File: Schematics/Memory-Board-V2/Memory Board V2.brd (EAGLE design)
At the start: 114 x 88.9 mm, 15 parts, among them IC4 27C128P, IC5 74HC174N, U1 GAL22V10D-DIP

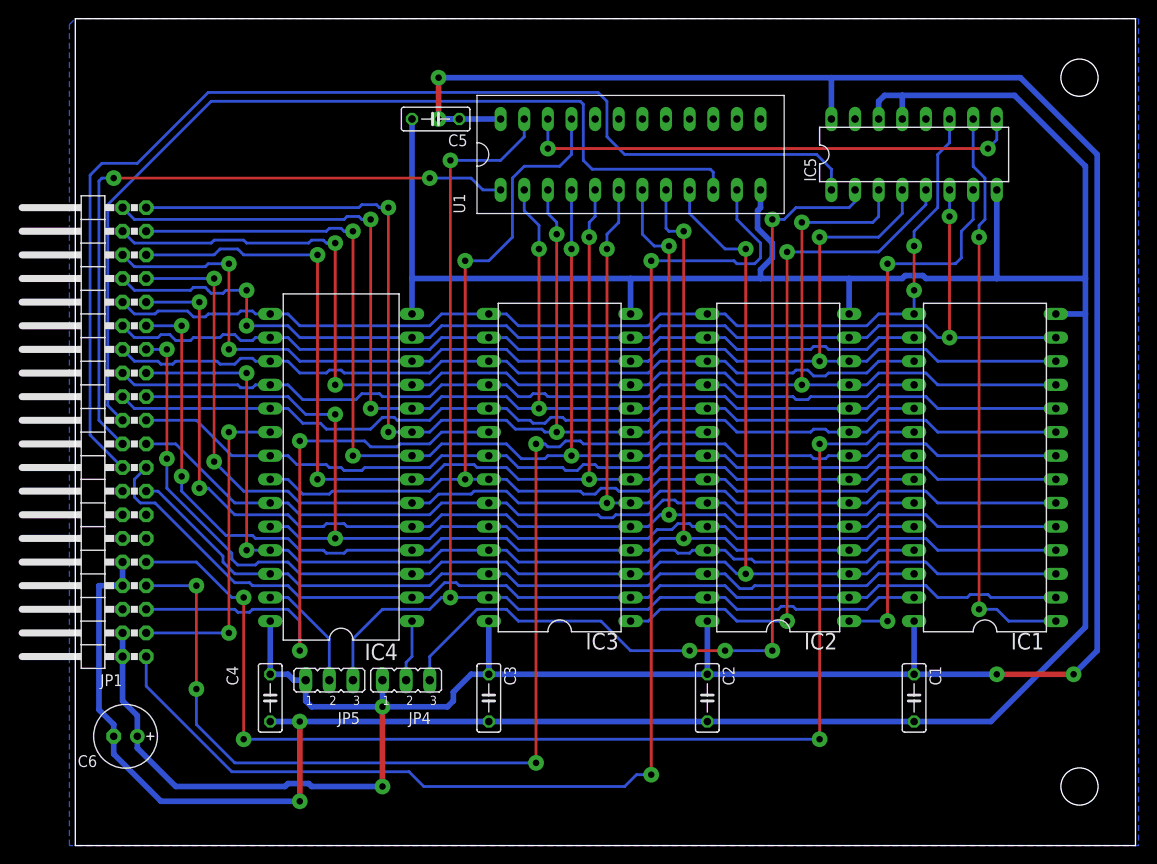
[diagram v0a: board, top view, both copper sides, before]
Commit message: Updated to have a formal Timer IRQ.  Currently this is T1 on the W65C22 on the GPIO card, so if you want to use it that card must be present.
The prebuilt ROM ToEVID.bin uses this card at 0xC040.

A couple of minor whoopsies have been fixed as well.
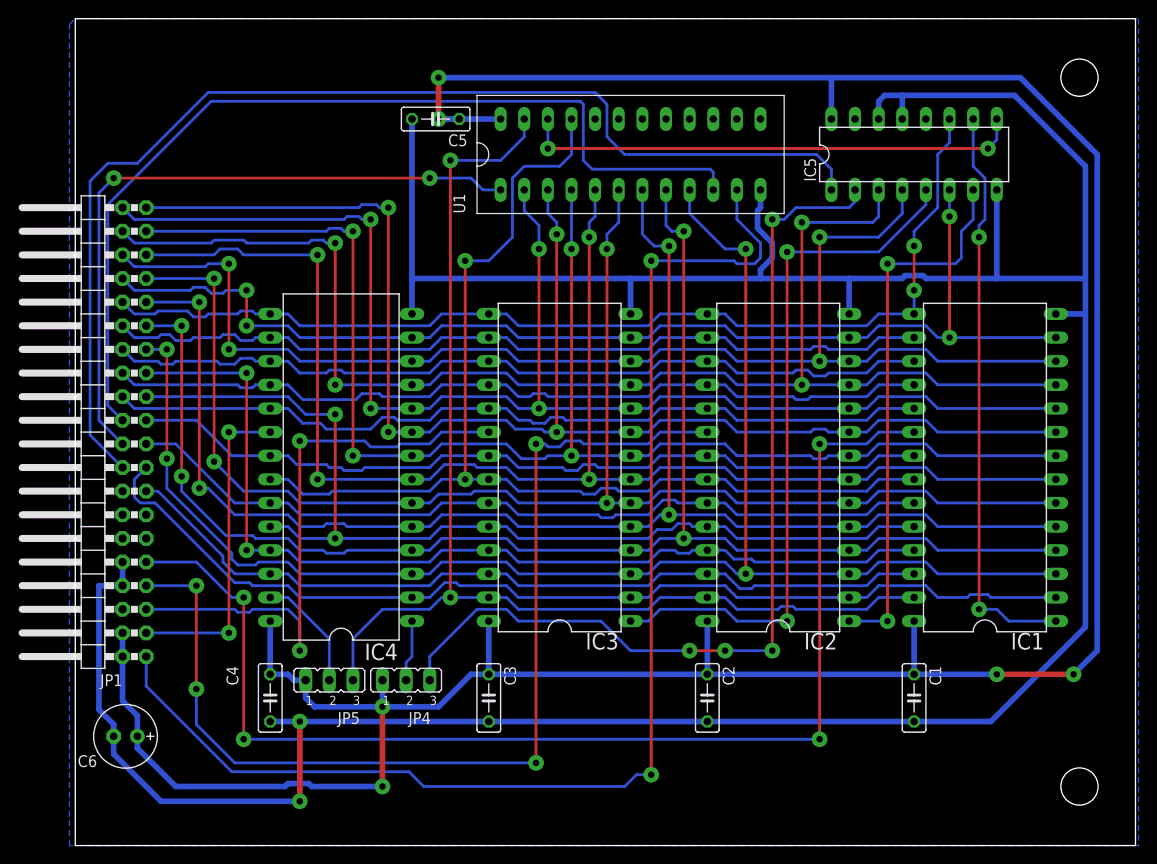
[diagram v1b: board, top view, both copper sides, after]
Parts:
- IC4: value 27C128P -> 27C128P/28C256
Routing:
- net PHI2: track 73.1 -> 72.4 mm
- net VCC: track 315.7 -> 315.0 mm
- net RESB: track 124.1 -> 123.6 mm
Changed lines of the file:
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@@
 <?xml version="1.0" encoding="utf-8"?>
 <!DOCTYPE eagle SYSTEM "eagle.dtd">
-<eagle version="6.6.0">
+<eagle version="6.5.0">
 <drawing>
 <settings>
@@
 <setting verticaltext="up"/>
 </settings>
-<grid distance="0.025" unitdist="inch" unit="mm" style="lines" multiple="1" display="no" altdistance="0.0125" altunitdist="inch" altunit="inch"/>
+<grid distance="0.0125" unitdist="inch" unit="inch" style="lines" multiple="1" display="no" altdistance="0.0125" altunitdist="inch" altunit="inch"/>
 <layers>
 <layer number="1" name="Top" color="4" fill="1" visible="yes" active="yes"/>
@@
 <attribute name="OC_FARNELL" value="unknown" x="97.79" y="40.64" size="1.778" layer="27" rot="R90" display="off"/>
 </element>
-<element name="IC4" library="microchip" package="DIL28-6" value="27C128P" x="28.575" y="40.64" rot="R90">
+<element name="IC4" library="microchip" package="DIL28-6" value="27C128P/28C256" x="28.575" y="40.64" smashed="yes" rot="R90">
 <attribute name="OC_NEWARK" value="unknown" x="28.575" y="40.64" size="1.778" layer="27" rot="R90" display="off"/>
 <attribute name="MPN" value="" x="28.575" y="40.64" size="1.778" layer="27" rot="R90" display="off"/>
 <attribute name="MF" value="" x="28.575" y="40.64" size="1.778" layer="27" rot="R90" display="off"/>
 <attribute name="OC_FARNELL" value="unknown" x="28.575" y="40.64" size="1.778" layer="27" rot="R90" display="off"/>
+<attribute name="NAME" x="34.671" y="21.717" size="1.778" layer="25" ratio="10" rot="R180"/>
+<attribute name="VALUE" x="33.3248" y="22.86" size="1.778" layer="27" ratio="10" rot="R90"/>
 </element>
 <element name="IC2" library="memory-hitachi" package="DIL28-6" value="" x="75.565" y="40.64" rot="R90">
@@
 <wire x1="86.995" y1="80.645" x2="86.36" y2="80.01" width="0.6096" layer="16"/>
 <wire x1="86.36" y1="80.01" x2="86.36" y2="78.105" width="0.6096" layer="16"/>
-<polygon width="0.3048" layer="16" isolate="0.4064">
+<polygon width="0.1524" layer="16" isolate="0.4064">
 <vertex x="0" y="88.9"/>
 <vertex x="114.3" y="88.9"/>
@@
 <wire x1="39.37" y1="33.02" x2="38.1" y2="31.75" width="0.3048" layer="16"/>
 <wire x1="38.1" y1="31.75" x2="36.195" y2="31.75" width="0.3048" layer="16"/>
-<wire x1="63.5" y1="70.485" x2="63.5" y2="66.3575" width="0.3048" layer="16"/>
-<wire x1="63.5" y1="66.3575" x2="63.8175" y2="66.04" width="0.3048" layer="16"/>
-<wire x1="63.8175" y1="66.04" x2="65.405" y2="66.04" width="0.3048" layer="16"/>
+<wire x1="63.5" y1="70.485" x2="63.5" y2="66.675" width="0.3048" layer="16"/>
+<wire x1="63.5" y1="66.675" x2="64.135" y2="66.04" width="0.3048" layer="16"/>
+<wire x1="64.135" y1="66.04" x2="65.405" y2="66.04" width="0.3048" layer="16"/>
 <via x="65.405" y="66.04" extent="1-16" drill="0.7" diameter="1.7"/>
 <wire x1="65.405" y1="66.04" x2="65.405" y2="33.02" width="0.3048" layer="1"/>
@@
 <wire x1="44.45" y1="24.13" x2="44.45" y2="18.415" width="0.6096" layer="16"/>
 <wire x1="44.45" y1="18.415" x2="42.545" y2="18.415" width="0.6096" layer="16"/>
-<wire x1="42.545" y1="18.415" x2="40.64" y2="16.51" width="0.6096" layer="16"/>
-<wire x1="40.64" y1="16.51" x2="40.64" y2="15.5575" width="0.6096" layer="16"/>
-<wire x1="40.64" y1="15.5575" x2="40.005" y2="14.9225" width="0.6096" layer="16"/>
-<wire x1="40.005" y1="14.9225" x2="33.02" y2="14.9225" width="0.6096" layer="16"/>
-<wire x1="33.02" y1="14.9225" x2="25.4" y2="14.9225" width="0.6096" layer="16"/>
-<wire x1="25.4" y1="14.9225" x2="24.765" y2="15.5575" width="0.6096" layer="16"/>
-<wire x1="24.765" y1="15.5575" x2="24.765" y2="17.78" width="0.6096" layer="16"/>
+<wire x1="42.545" y1="18.415" x2="39.0525" y2="14.9225" width="0.6096" layer="16"/>
+<wire x1="39.0525" y1="14.9225" x2="33.02" y2="14.9225" width="0.6096" layer="16"/>
+<wire x1="33.02" y1="14.9225" x2="25.7175" y2="14.9225" width="0.6096" layer="16"/>
+<wire x1="25.7175" y1="14.9225" x2="24.765" y2="15.875" width="0.6096" layer="16"/>
+<wire x1="24.765" y1="15.875" x2="24.765" y2="17.78" width="0.6096" layer="16"/>
 <wire x1="33.02" y1="17.78" x2="33.02" y2="14.9225" width="0.6096" layer="16"/>
 <wire x1="24.765" y1="17.78" x2="23.495" y2="17.78" width="0.6096" layer="16"/>
@@
 <contactref element="U1" pad="1-I/CLK"/>
 <wire x1="5.08" y1="43.18" x2="2.54" y2="45.72" width="0.3048" layer="16"/>
-<wire x1="2.54" y1="45.72" x2="2.54" y2="71.4375" width="0.3048" layer="16"/>
-<wire x1="2.54" y1="71.4375" x2="2.8575" y2="71.755" width="0.3048" layer="16"/>
-<wire x1="2.8575" y1="71.755" x2="4.1275" y2="71.755" width="0.3048" layer="16"/>
+<wire x1="2.54" y1="45.72" x2="2.54" y2="70.1675" width="0.3048" layer="16"/>
+<wire x1="2.54" y1="70.1675" x2="4.1275" y2="71.755" width="0.3048" layer="16"/>
 <via x="4.1275" y="71.755" extent="1-16" drill="0.7" diameter="1.7"/>
 <wire x1="4.1275" y1="71.755" x2="38.1" y2="71.755" width="0.3048" layer="1"/>
@@
 <contactref element="IC5" pad="1"/>
 <wire x1="5.08" y1="40.64" x2="1.5875" y2="44.1325" width="0.3048" layer="16"/>
-<wire x1="1.5875" y1="44.1325" x2="1.5875" y2="72.0725" width="0.3048" layer="16"/>
-<wire x1="1.5875" y1="72.0725" x2="2.8575" y2="73.3425" width="0.3048" layer="16"/>
-<wire x1="2.8575" y1="73.3425" x2="6.6675" y2="73.3425" width="0.3048" layer="16"/>
+<wire x1="1.5875" y1="44.1325" x2="1.5875" y2="71.4375" width="0.3048" layer="16"/>
+<wire x1="1.5875" y1="71.4375" x2="3.4925" y2="73.3425" width="0.3048" layer="16"/>
+<wire x1="3.4925" y1="73.3425" x2="6.6675" y2="73.3425" width="0.3048" layer="16"/>
 <wire x1="6.6675" y1="73.3425" x2="14.2875" y2="80.9625" width="0.3048" layer="16"/>
-<wire x1="14.2875" y1="80.9625" x2="56.1975" y2="80.9625" width="0.3048" layer="16"/>
-<wire x1="56.1975" y1="80.9625" x2="57.15" y2="80.01" width="0.3048" layer="16"/>
-<wire x1="57.15" y1="80.01" x2="57.15" y2="76.2" width="0.3048" layer="16"/>
+<wire x1="14.2875" y1="80.9625" x2="55.88" y2="80.9625" width="0.3048" layer="16"/>
+<wire x1="55.88" y1="80.9625" x2="57.15" y2="79.6925" width="0.3048" layer="16"/>
+<wire x1="57.15" y1="79.6925" x2="57.15" y2="76.2" width="0.3048" layer="16"/>
 <wire x1="57.15" y1="76.2" x2="59.055" y2="74.295" width="0.3048" layer="16"/>
 <wire x1="59.055" y1="74.295" x2="79.6925" y2="74.295" width="0.3048" layer="16"/>
